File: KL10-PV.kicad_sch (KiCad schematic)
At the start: 0 parts

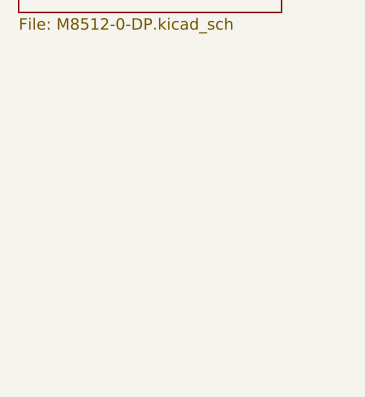
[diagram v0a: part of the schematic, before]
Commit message: Added DP02
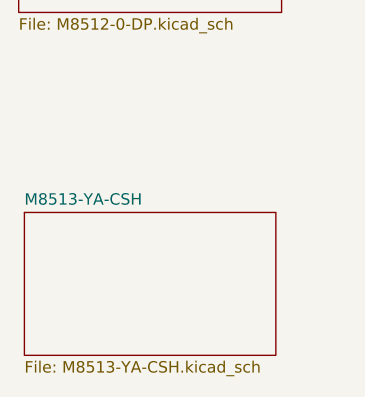
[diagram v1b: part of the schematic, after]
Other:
- added sheet M8513-YA-CSH (M8513-YA-CSH.kicad_sch)
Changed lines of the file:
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@@
+    )
+  )
+  (sheet (at 27.305 75.565) (size 27.94 15.875) (fields_autoplaced)
+    (stroke (width 0.1524) (type solid) (color 0 0 0 0))
+    (fill (color 0 0 0 0.0000))
+    (property "Sheet name" "M8513-YA-CSH" (id 0) (at 27.305 74.8534 0)
+      (effects (font (size 1.27 1.27)) (justify left bottom))
+    )
+    (property "Sheet file" "M8513-YA-CSH.kicad_sch" (id 1) (at 27.305 92.0246 0)
+      (effects (font (size 1.27 1.27)) (justify left top))
     )
   )
@@
     (path "/" (page "1"))
     (path "/125b7ac6-58f8-4648-989a-7cb26078849e" (page "2"))
+    (path "/7f435098-d85b-42cc-8461-7690d9182834" (page "5"))
     (path "/125b7ac6-58f8-4648-989a-7cb26078849e/0d0df2ac-f3f7-482e-ba7c-5f666b048a62" (page ""))
     (path "/125b7ac6-58f8-4648-989a-7cb26078849e/e53a1afb-1269-4ccc-9d39-72635457c7f7" (page ""))
   )
   (symbol_instances
+    (path "/125b7ac6-58f8-4648-989a-7cb26078849e/e53a1afb-1269-4ccc-9d39-72635457c7f7/8f8d41cd-942f-44e5-8323-26ec1bc7d76b"
+      (reference "E11") (unit 1) (value "MC10101") (footprint "")
+    )
+    (path "/125b7ac6-58f8-4648-989a-7cb26078849e/e53a1afb-1269-4ccc-9d39-72635457c7f7/7f53f9c5-42a9-4a18-b3e9-1febfec9f0f2"
+      (reference "E11") (unit 2) (value "MC10101") (footprint "")
+    )
+    (path "/125b7ac6-58f8-4648-989a-7cb26078849e/e53a1afb-1269-4ccc-9d39-72635457c7f7/0ef9e558-bb22-4c9a-a897-692a81d8f073"
+      (reference "E11") (unit 4) (value "MC10101") (footprint "")
+    )
+    (path "/125b7ac6-58f8-4648-989a-7cb26078849e/e53a1afb-1269-4ccc-9d39-72635457c7f7/9170e5db-e7eb-45f0-8f21-bae0746d54a8"
+      (reference "E13") (unit 1) (value "MC10141") (footprint "")
+    )
+    (path "/125b7ac6-58f8-4648-989a-7cb26078849e/e53a1afb-1269-4ccc-9d39-72635457c7f7/5acaa071-18e3-4dc9-8349-7343bb423819"
+      (reference "E15") (unit 1) (value "MC10141") (footprint "")
+    )
+    (path "/125b7ac6-58f8-4648-989a-7cb26078849e/e53a1afb-1269-4ccc-9d39-72635457c7f7/be04f6b9-8eeb-481b-b86a-40942fea1f30"
+      (reference "E20") (unit 1) (value "MC10101") (footprint "")
+    )
+    (path "/125b7ac6-58f8-4648-989a-7cb26078849e/e53a1afb-1269-4ccc-9d39-72635457c7f7/366ca6df-dd19-4d75-ba3f-9f7b938b7067"
+      (reference "E20") (unit 2) (value "MC10101") (footprint "")
+    )
+    (path "/125b7ac6-58f8-4648-989a-7cb26078849e/e53a1afb-1269-4ccc-9d39-72635457c7f7/a520edcf-b2fc-495c-ad52-5364b381b564"
+      (reference "E20") (unit 3) (value "MC10101") (footprint "")
+    )
+    (path "/125b7ac6-58f8-4648-989a-7cb26078849e/e53a1afb-1269-4ccc-9d39-72635457c7f7/930fc5ba-bd30-4b2c-9652-2dad589018b7"
+      (reference "E20") (unit 4) (value "MC10101") (footprint "")
+    )
+    (path "/125b7ac6-58f8-4648-989a-7cb26078849e/e53a1afb-1269-4ccc-9d39-72635457c7f7/395f7a2b-2b95-4c06-b1ed-1275cdf09d72"
+      (reference "E24") (unit 1) (value "MC10101") (footprint "")
+    )
+    (path "/125b7ac6-58f8-4648-989a-7cb26078849e/e53a1afb-1269-4ccc-9d39-72635457c7f7/c71b53c6-2999-49cf-9bd8-62260d478fcc"
+      (reference "E24") (unit 2) (value "MC10101") (footprint "")
+    )
+    (path "/125b7ac6-58f8-4648-989a-7cb26078849e/e53a1afb-1269-4ccc-9d39-72635457c7f7/3701038a-dc8f-49de-aa3f-d697cfb70bb8"
+      (reference "E24") (unit 3) (value "MC10101") (footprint "")
+    )
+    (path "/125b7ac6-58f8-4648-989a-7cb26078849e/e53a1afb-1269-4ccc-9d39-72635457c7f7/36f208af-fa33-4dfa-8680-821088f3515c"
+      (reference "E24") (unit 4) (value "MC10101") (footprint "")
+    )
+    (path "/125b7ac6-58f8-4648-989a-7cb26078849e/e53a1afb-1269-4ccc-9d39-72635457c7f7/8e2eb39b-aa26-4b34-a20f-e9dc4b927fab"
+      (reference "E25") (unit 1) (value "MC10141") (footprint "")
+    )
+    (path "/125b7ac6-58f8-4648-989a-7cb26078849e/e53a1afb-1269-4ccc-9d39-72635457c7f7/9942ec2f-039f-4d83-a339-abe9986b4664"
+      (reference "E32") (unit 1) (value "MC10141") (footprint "")
+    )
+    (path "/125b7ac6-58f8-4648-989a-7cb26078849e/e53a1afb-1269-4ccc-9d39-72635457c7f7/b2881a38-0283-4be2-a47d-af705a727954"
+      (reference "E35") (unit 1) (value "MC10174") (footprint "")
+    )
+    (path "/125b7ac6-58f8-4648-989a-7cb26078849e/e53a1afb-1269-4ccc-9d39-72635457c7f7/42f2285e-6e97-40eb-925e-f784cb733bf1"
+      (reference "E38") (unit 1) (value "MC10101") (footprint "")
+    )
+    (path "/125b7ac6-58f8-4648-989a-7cb26078849e/e53a1afb-1269-4ccc-9d39-72635457c7f7/165541be-ccaf-46a1-a88f-337dc353a710"
+      (reference "E38") (unit 2) (value "MC10101") (footprint "")
+    )
+    (path "/125b7ac6-58f8-4648-989a-7cb26078849e/e53a1afb-1269-4ccc-9d39-72635457c7f7/67d34cf7-0cf1-41e3-b155-d5900a891f55"
+      (reference "E38") (unit 4) (value "MC10101") (footprint "")
+    )
+    (path "/125b7ac6-58f8-4648-989a-7cb26078849e/e53a1afb-1269-4ccc-9d39-72635457c7f7/aafd2bc0-5c6e-4351-934b-41190f6068c2"
+      (reference "E45") (unit 1) (value "MC10174") (footprint "")
+    )
+    (path "/125b7ac6-58f8-4648-989a-7cb26078849e/e53a1afb-1269-4ccc-9d39-72635457c7f7/dab00188-e63d-4c9b-b646-191b77828ddf"
+      (reference "E48") (unit 1) (value "MC10174") (footprint "")
+    )
+    (path "/125b7ac6-58f8-4648-989a-7cb26078849e/e53a1afb-1269-4ccc-9d39-72635457c7f7/9ae1382c-26c4-41ce-8f1f-db21d7e88ad6"
+      (reference "E49") (unit 1) (value "MC10164") (footprint "")
+    )
+    (path "/125b7ac6-58f8-4648-989a-7cb26078849e/e53a1afb-1269-4ccc-9d39-72635457c7f7/dc47d78f-ffc4-46f5-97a5-4b9135225541"
+      (reference "E55") (unit 1) (value "MC10164") (footprint "")
+    )
+    (path "/125b7ac6-58f8-4648-989a-7cb26078849e/e53a1afb-1269-4ccc-9d39-72635457c7f7/183ce7c8-a7f5-421a-95e8-f0a434c8473a"
+      (reference "E56") (unit 1) (value "MC10164") (footprint "")
+    )
+    (path "/125b7ac6-58f8-4648-989a-7cb26078849e/e53a1afb-1269-4ccc-9d39-72635457c7f7/7ae22fb7-ff4b-4829-9c6e-5be5a40c61c9"
+      (reference "E60") (unit 1) (value "MC10101") (footprint "")
+    )
+    (path "/125b7ac6-58f8-4648-989a-7cb26078849e/e53a1afb-1269-4ccc-9d39-72635457c7f7/56acdca2-c4b2-48b8-a04d-777504b984e7"
+      (reference "E60") (unit 2) (value "MC10101") (footprint "")
+    )
+    (path "/125b7ac6-58f8-4648-989a-7cb26078849e/e53a1afb-1269-4ccc-9d39-72635457c7f7/de28e8ca-da94-4b17-90a6-6fd14251e824"
+      (reference "E60") (unit 4) (value "MC10101") (footprint "")
+    )
     (path "/125b7ac6-58f8-4648-989a-7cb26078849e/0d0df2ac-f3f7-482e-ba7c-5f666b048a62/0f39e560-9336-4a48-a641-fec45e29a92d"
       (reference "E?") (unit 1) (value "MC10141") (footprint "")

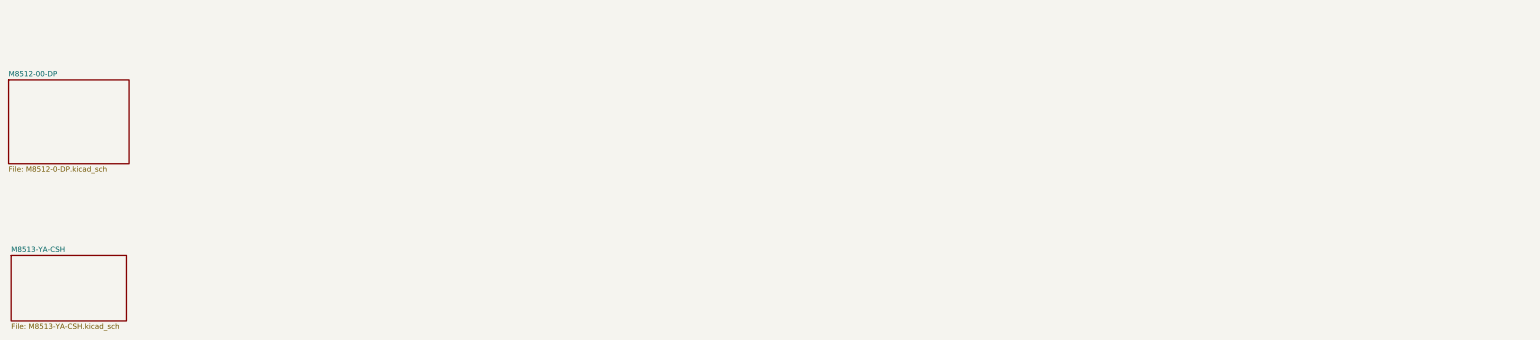
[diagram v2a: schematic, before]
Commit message: EDP is "done" but there is still much work to do to standardize and set up netlist export and verilog creation
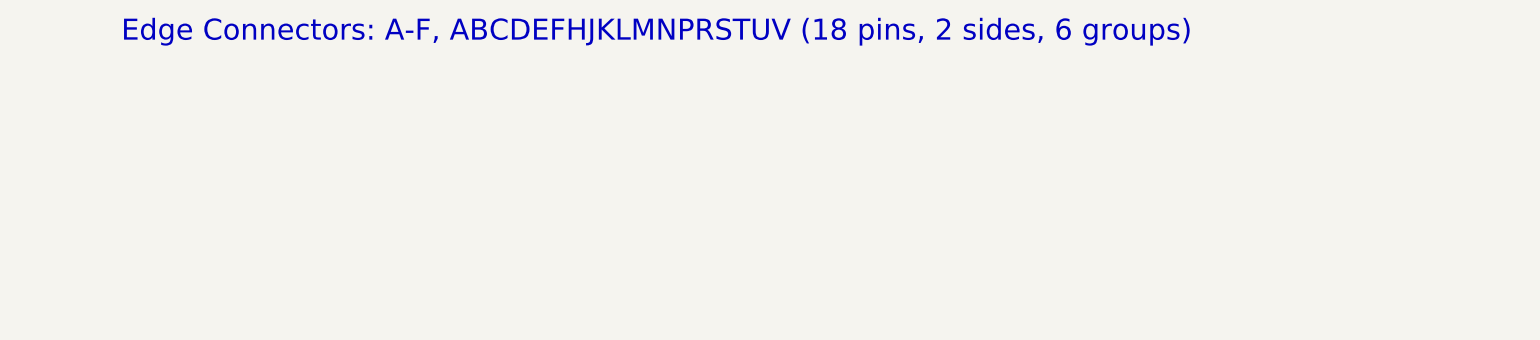
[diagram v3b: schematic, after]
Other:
- removed sheet M8512-00-DP
- removed sheet M8513-YA-CSH
- note added: "Edge Connectors: A-F, ABCDEFHJKLMNPRSTUV (18 pins, 2 sides, 6 groups)"
- title: KL10-PV CPU -> DATA PATH AR REGISTER
